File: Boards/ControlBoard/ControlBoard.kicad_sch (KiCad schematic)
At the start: 0 parts

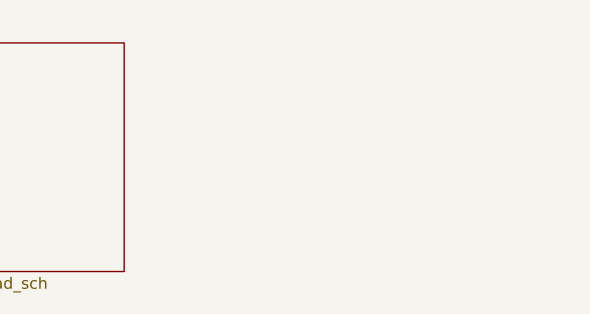
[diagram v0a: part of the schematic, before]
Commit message: Add Filter Caps To ADC Control Board IC
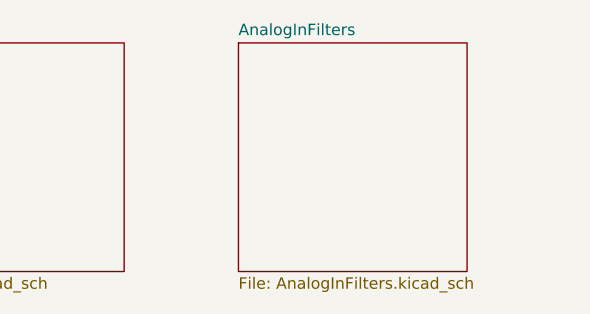
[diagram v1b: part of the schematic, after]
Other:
- added sheet AnalogInFilters (AnalogInFilters.kicad_sch)
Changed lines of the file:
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@@
+	)
+	(sheet
+		(at 215.9 25.4)
+		(size 25.4 25.4)
+		(exclude_from_sim no)
+		(in_bom yes)
+		(on_board yes)
+		(dnp no)
+		(fields_autoplaced yes)
+		(stroke
+			(width 0.1524)
+			(type solid)
+		)
+		(fill
+			(color 0 0 0 0.0000)
+		)
+		(property "Sheetname" "AnalogInFilters"
+			(at 215.9 24.6884 0)
+			(effects
+				(font
+					(size 1.27 1.27)
+				)
+				(justify left bottom)
+			)
+		)
+		(property "Sheetfile" "AnalogInFilters.kicad_sch"
+			(at 215.9 51.3846 0)
+			(effects
+				(font
+					(size 1.27 1.27)
+				)
+				(justify left top)
+			)
+		)
+		(instances
+			(project "ControlBoard"
+				(path "/66e49eb5-2741-49e2-b48a-baf482488ca8"
+					(page "7")
+				)
+			)
+		)
 	)
 	(sheet
